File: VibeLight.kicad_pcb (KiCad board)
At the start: 2 copper layers, 28.1 x 34 mm, 42 parts, among them J1 Conn_ARM_SWD_TagConnect_TC203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, SW1 SW_Push, SW2 SW_Push

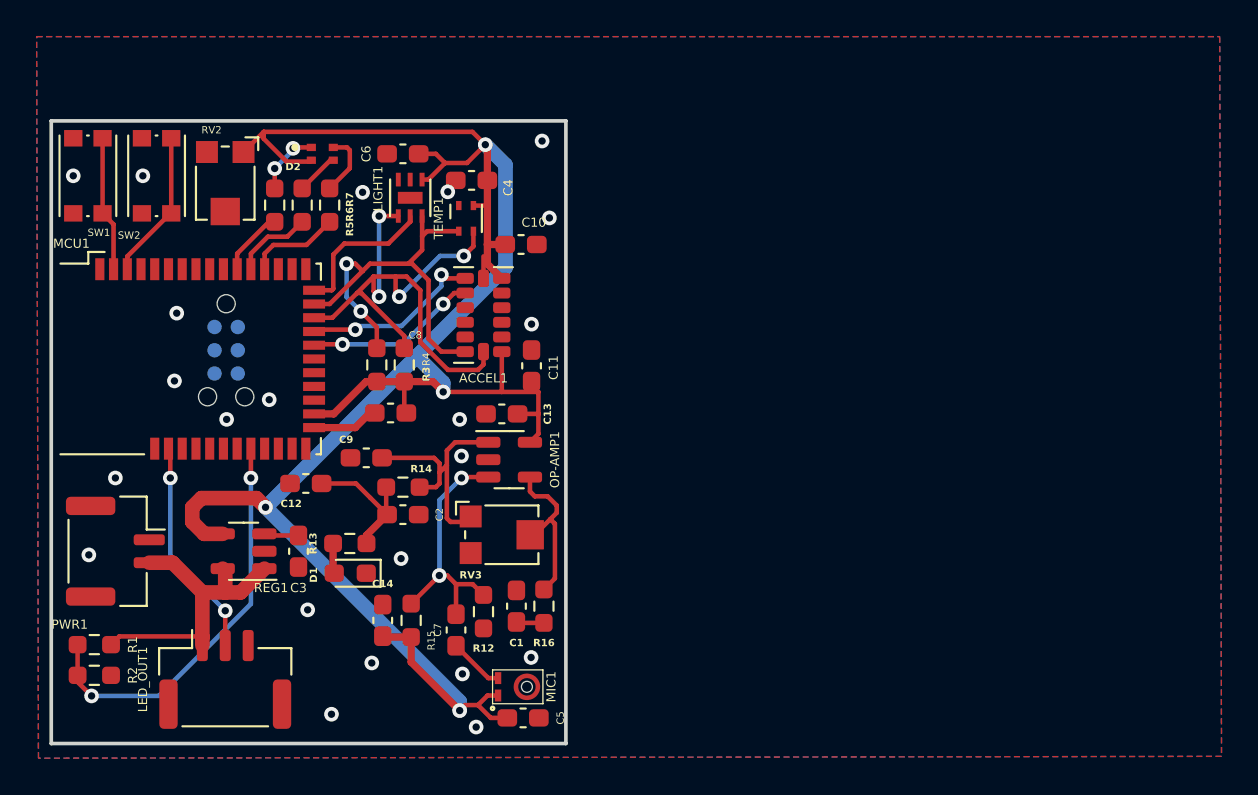
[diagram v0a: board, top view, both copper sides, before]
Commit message: update
updated in accordance with 8/5 schem notes
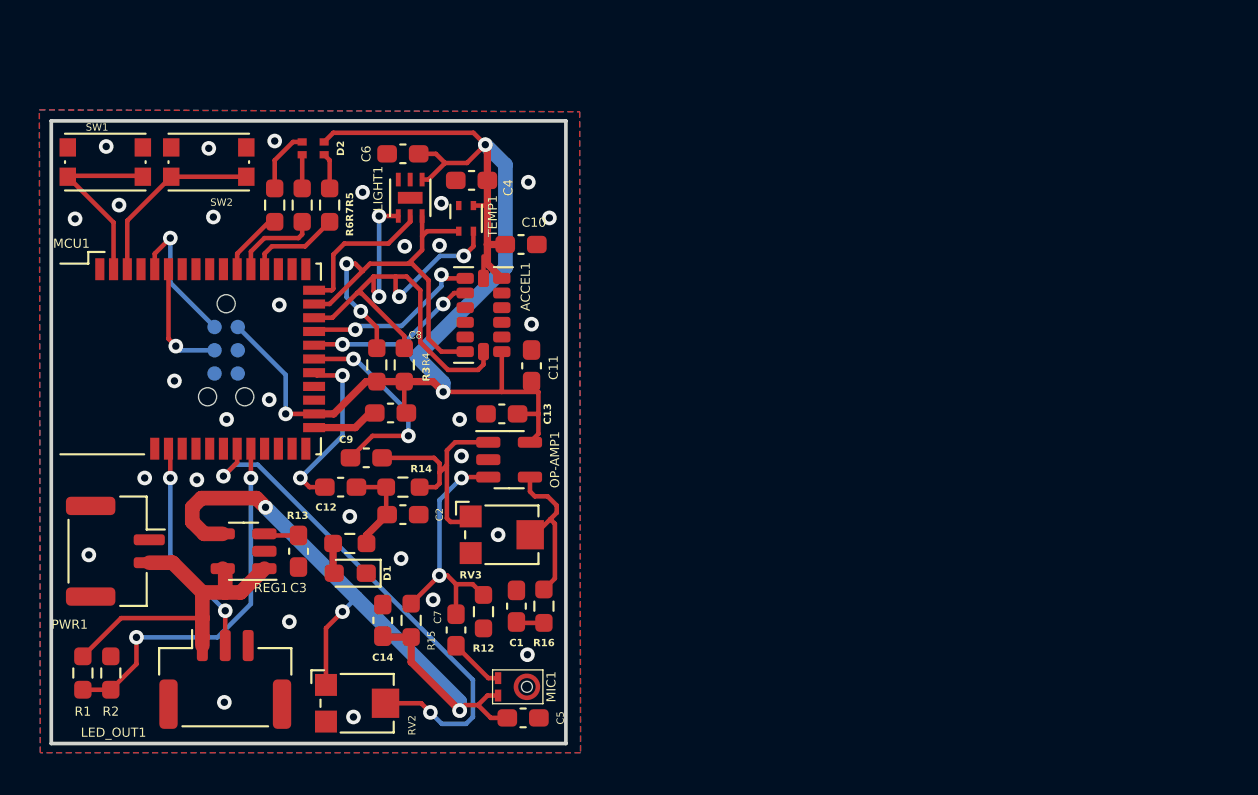
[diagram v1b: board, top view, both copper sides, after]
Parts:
- moved RV2 29.2 mm to (34.8, 50.8), turned to 0 degrees
- moved R5 3.00 mm to (33.2, 23.6)
- moved SW2 2.95 mm to (26.6, 21.2), turned to 180 degrees
- moved C12 1.91 mm to (33.8, 39.0)
- moved R1 1.67 mm to (19.7, 49.1), turned to -90 degrees
- moved R7 1.50 mm to (31.7, 23.6)
- moved R6 1.50 mm to (30.2, 23.6)
- moved SW1 1.21 mm to (20.9, 21.2), turned to 180 degrees
- moved R2 0.91 mm to (21.2, 49.1), turned to 90 degrees
- moved D2 0.58 mm to (32.3, 20.5), turned to 180 degrees
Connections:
- MCU1 pad 22: unconnected-(MCU1-SIO_03/AIN1-Pad22) -> /Audio Input/RAW
- MCU1 pad 23: unconnected-(MCU1-SIO_02/AIN0-Pad23) -> /Audio Input/FIL
- MCU1 pad 33: unconnected-(MCU1-SIO_30/AIN6-Pad33) -> /MCU/Intensity_Dial
- R5 pad 2: Net-(MCU1-SIO_14) -> Net-(MCU1-SIO_11)
- R6 pad 2: Net-(MCU1-SIO_12) -> Net-(MCU1-SIO_14)
- R7 pad 1: Net-(MCU1-SIO_11) -> Net-(MCU1-SIO_12)
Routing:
- net /MCU/Intensity_Dial: track 0.00 -> 28.0 mm, vias 0 -> 2
- net /Audio Input/RAW: track 0.00 -> 11.3 mm, vias 0 -> 2
- net /Audio Input/FIL: track 0.00 -> 9.71 mm, vias 0 -> 2
- net /MCU/SWDIO: track 0.00 -> 7.91 mm, vias 0 -> 1
- net +3V3: track 118.9 -> 111.9 mm, vias 4 -> 6
- net /MCU/SWCLK: track 0.00 -> 6.57 mm, vias 0 -> 1
- net /MCU/SW1: track 7.40 -> 10.2 mm
- net Net-(C12-Pad1): track 7.84 -> 5.19 mm
- net /MCU/SW2: track 8.17 -> 10.1 mm
- net /BATT+: track 17.2 -> 19.2 mm
- net Net-(MCU1-SIO_31/AIN7): track 22.4 -> 20.4 mm
- net Net-(D2-BK): track 3.51 -> 1.84 mm
- net Net-(D2-RK): track 3.62 -> 1.96 mm, vias 2 -> 0
- net Net-(D2-GK): track 2.34 -> 3.45 mm
- net GND: vias 22 -> 30

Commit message: updated GND vias and unconnected errors
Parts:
- moved C3 2.11 mm to (32.3, 40.5), turned to 0 degrees
- moved R1 1.08 mm to (20.5, 48.4), turned to 180 degrees
- moved R2 1.08 mm to (20.5, 49.9), turned to 0 degrees
- moved C14 0.93 mm to (36.1, 47.2)
- moved R15 0.93 mm to (37.6, 47.2)
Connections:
- LIGHT1 pad 7: (no net) -> GND
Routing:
- net GND: track 3.64 -> 20.6 mm, vias 30 -> 23
- net +3V3: track 111.9 -> 124.2 mm, vias 6 -> 7
- net Net-(MCU1-SIO_31/AIN7): track 20.4 -> 24.7 mm
- net /Audio Input/FIL: track 9.71 -> 11.0 mm
- net Net-(OP-AMP1-+): track 14.0 -> 14.9 mm
- net /BATT+: track 19.2 -> 18.6 mm
- net /SCL: track 32.9 -> 32.5 mm, vias 4 -> 3

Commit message: R1 Release package
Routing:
- net +3V3: track 124.2 -> 118.1 mm
- net Net-(OP-AMP1--): track 9.10 -> 6.69 mm
- net /Audio Input/FIL: track 11.0 -> 9.81 mm
